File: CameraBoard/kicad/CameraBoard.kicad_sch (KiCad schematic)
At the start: 57 parts, among them Q1 SUD08P06-155L, Q2 SUD08P06-155L, Q3 SUD08P06-155L, U1 MP2659GQ-0000-Z

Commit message: Schematic and PCB Changes
-Added symbols and footprints to library
-Changed a couple mosfets and the thermistor for better fits
-Added more description to connectors
-Added power flags
-Edited IC symbols to match datasheets
-Made sure all components had values showing
-Added descriptive names to connectors on PCB
-Rearranged PCB after switching out some components footprints
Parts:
- removed D4: D_MBRS340T3G, Diode_SMD:D_SMC, symbol Diode:MBRS340
- removed Q1, Q3: SUD08P06-155L, Package_TO_SOT_SMD:TO-252-2, symbol Transistor_FET:SUD08P06-155L
- removed U2: (no value), CameraBoard:LM2678SD-12_NOPB, symbol CameraBoard-eagle-import:LM2678SD-12/NOPB
- added D4: VS-6TQ045S-M3, oresat-diodes:VS6TQ045SM3, symbol oresat-diodes:VS-6TQ045S-M3
- added Q1: DMG3404L-7, oresat-transistors:DMG3404L_DIO, symbol oresat-transistors:DMG3404L-7
- added Q3: AOD4185, oresat-transistors:TO252_AOS-M, symbol oresat-transistors:AOD4185
- added TP10, TP11, TP4, TP5, TP6, TP7, TP8, TP9: Test-Point, oresat-misc:TestPoint-0.75mm-th, symbol Connector:TestPoint_Square
- added U2: LM2678SD-ADJ/NOPB, psas-footprints:SRC14A, symbol psas-ics:LM2678SD-ADJ_NOPB
- D5: value LED_Small_Filled -> GRN
- L1: value 784770220 -> 22uh; footprint CameraBoard:784770220 -> Inductor_SMD:L_Vishay_IHLP-4040; DPN 732-6785-1-ND -> 541-IHLP4040EDER220M5ACT-ND; MPN 74477110 -> IHLP4040EDER220M5A; Manufacturer_Name Würth Elektronik -> Vishay Dale
- R13: value 3.3k -> 10k
- TH1: footprint oresat-misc:THRMC1608X95N -> Resistor_THT:R_Axial_DIN0204_L3.6mm_D1.6mm_P2.54mm_Vertical; DPN 490-16279-1-ND -> 495-2153-ND; MPN NCU18XH103F60RB -> B57871S0103F001; Manufacturer_Name Murata Electronics -> TDK
- TP1, TP2, TP3: footprint CameraBoard:2MM-TEST-POINT -> oresat-misc:TestPoint-0.75mm-th; symbol psas-testpoint:Test-Point -> Connector:TestPoint_Square
- U1: symbol psas-libraries:MP2659GQ-0000-Z -> psas-ics:MP2659GQ-0000-Z
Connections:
- net +12V: now also U2.7 (FB)
- net BATT+: now also Q3.3 (S)
- net GND: now also U1.[5-7] (PGND), D4.3 (A), Q1.2 (S), U2.9 (GND); no longer U1.5 (PGND_1), U1.6 (PGND_2), U1.7 (PGND_3)
- net VBATT: now also Q2.3 (S), Q3.2 (D); no longer Q2.2 (D)
- net at C1.1, C3.1, C4.1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: now also Q2.2 (D), U2.[2,3] (Vin); no longer Q2.3 (S)
- net at C7.2: now also U2.4 (BOOST)
- net at TP1.1: now also U2.8 (ON)
- net at R11.2, R14.1: now also Q3.1 (G)
- net at Q2.1 (G), R1.2: now also Q1.3 (D)
- net at JP13.3 (Pin_3): now also TP11.1
- net at JP1.2 (Pin_2), R2.1: now also Q1.1 (G)
- net at JP6.3 (Pin_3): now also TP4.1
- net at JP7.3 (Pin_3): now also TP5.1
- net at JP12.3 (Pin_3): now also TP10.1
- net at JP11.3 (Pin_3): now also TP9.1
- net at JP8.3 (Pin_3): now also TP6.1
- net at JP10.3 (Pin_3): now also TP8.1
- net at JP9.3 (Pin_3): now also TP7.1
- net SOUT: no longer names the net of C7.1, L1.1
- net SOUT: now also D4.2 (K), U2.[12-14] (SW)
- no-connect marks 10 -> 2
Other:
- note added: "(12, 14.4, 16.8) V."
- note added: "Comp selection: -Datasheet called for polarized -The diode has 6A rating"
- note added: "Enabled by RR; turns on with cams."
- note added: "Enables system; 3.3V from Telemetrum Sender."
- note added: "Pulls 0.15A"
- note added: "Pulls 1.77A"
- note removed: "Comp selection: -Datasheet called for polarized -The diode has 4A rating"
- note removed: "Wired into 12V because it was easy; might be better directly to vbatt."
- moved on the sheet: C1, C10, C11, C12, C13, C3, C4, C5, C6, C7, C8, C9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

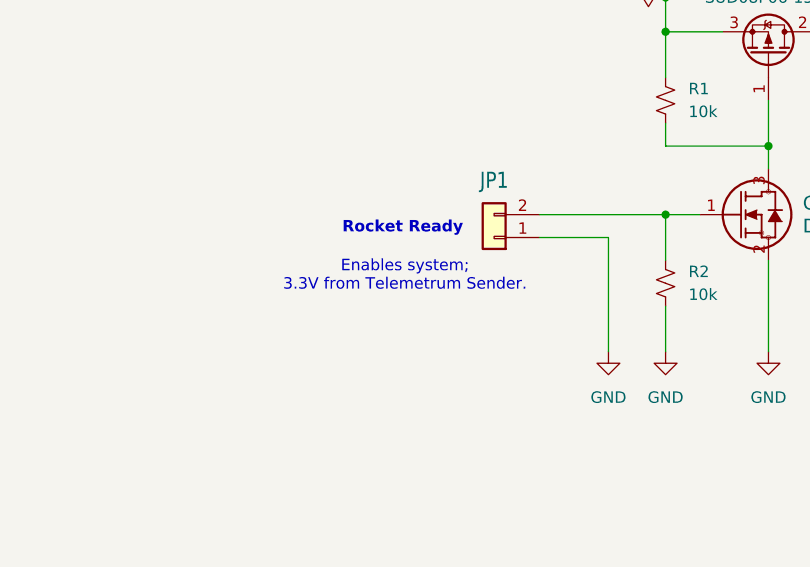
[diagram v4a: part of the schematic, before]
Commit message: Description Fix
Changed "3.3V" to "5V"
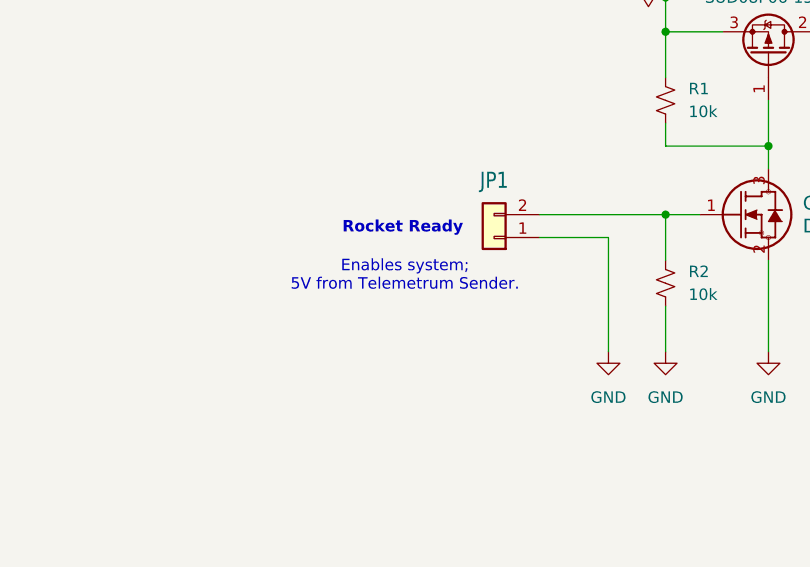
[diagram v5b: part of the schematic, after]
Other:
- note added: "Enables system; 5V from Telemetrum Sender."
- note removed: "Enables system; 3.3V from Telemetrum Sender."
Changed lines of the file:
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@@
 		)
 	)
-	(text "Enables system;\n3.3V from Telemetrum Sender."
+	(text "Enables system;\n5V from Telemetrum Sender."
 		(exclude_from_sim no)
 		(at 34.544 206.248 0)
